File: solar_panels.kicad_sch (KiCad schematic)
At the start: 0 parts

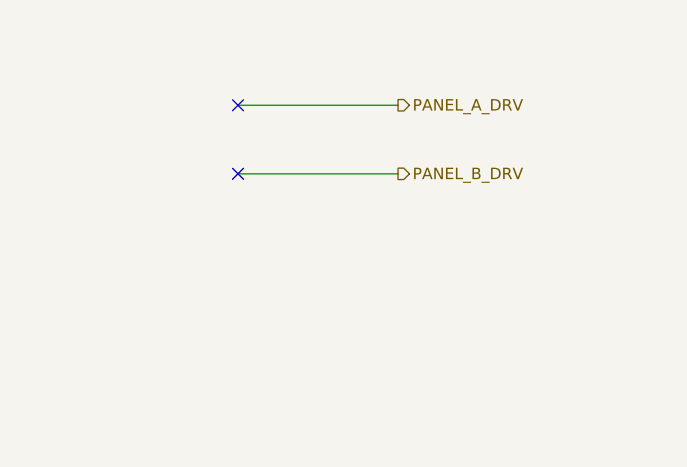
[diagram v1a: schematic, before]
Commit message: Adding in connections to schematic
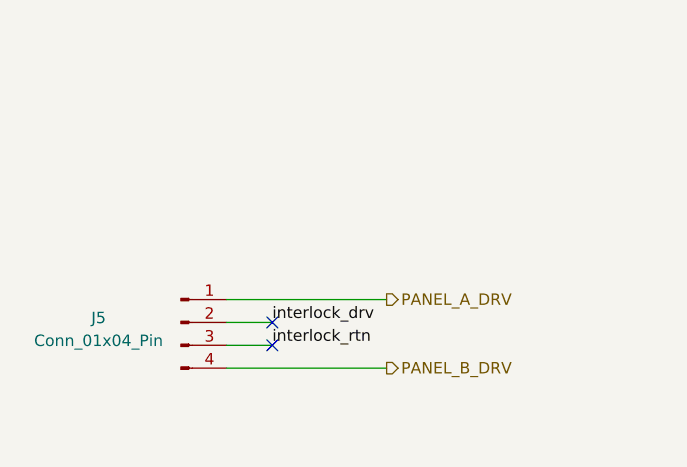
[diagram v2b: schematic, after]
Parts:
- added J5: Conn_01x04_Pin, symbol Connector:Conn_01x04_Pin
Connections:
- net PANEL_A_DRV: now also J5.1 (Pin_1)
- net PANEL_B_DRV: now also J5.4 (Pin_4)
- new net interlock_drv: J5.2 (Pin_2)
- new net interlock_rtn: J5.3 (Pin_3)
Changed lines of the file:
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@@
 	(paper "A4")
 	(no_connect
-		(at 134.62 73.66)
+		(at 138.43 97.79)
 	)
 	(no_connect
-		(at 134.62 81.28)
+		(at 138.43 100.33)
 	)
 	(wire
 		(pts
-			(xy 134.62 81.28) (xy 152.4 81.28)
+			(xy 133.35 102.87) (xy 151.13 102.87)
 		)
 		(stroke
@@
 	(wire
 		(pts
-			(xy 134.62 73.66) (xy 152.4 73.66)
+			(xy 133.35 95.25) (xy 151.13 95.25)
 		)
 		(stroke
@@
 		)
 	)
+	(wire
+		(pts
+			(xy 133.35 100.33) (xy 138.43 100.33)
+		)
+		(stroke
+			(width 0)
+			(type default)
+		)
+	)
+	(wire
+		(pts
+			(xy 133.35 97.79) (xy 138.43 97.79)
+		)
+		(stroke
+			(width 0)
+			(type default)
+		)
+	)
+	(label "interlock_drv"
+		(at 138.43 97.79 0)
+		(effects
+			(font
+				(size 1.27 1.27)
+			)
+			(justify left bottom)
+		)
+	)
+	(label "interlock_rtn"
+		(at 138.43 100.33 0)
+		(effects
+			(font
+				(size 1.27 1.27)
+			)
+			(justify left bottom)
+		)
+	)
 	(hierarchical_label "PANEL_A_DRV"
 		(shape output)
-		(at 152.4 73.66 0)
+		(at 151.13 95.25 0)
 		(effects
 			(font
@@
 	(hierarchical_label "PANEL_B_DRV"
 		(shape output)
-		(at 152.4 81.28 0)
+		(at 151.13 102.87 0)
 		(effects
 			(font
@@
 		)
 	)
+	(symbol
+		(lib_id "Connector:Conn_01x04_Pin")
+		(at 128.27 97.79 0)
+		(unit 1)
+		(exclude_from_sim no)
+		(in_bom yes)
+		(on_board yes)
+		(dnp no)
+		(property "Reference" "J5"
+			(at 119.126 97.282 0)
+			(effects
+				(font
+					(size 1.27 1.27)
+				)
+			)
+		)
+		(property "Value" "Conn_01x04_Pin"
+			(at 119.126 99.822 0)
+			(effects
+				(font
+					(size 1.27 1.27)
+				)
+			)
+		)
+		(property "Footprint" ""
+			(at 128.27 97.79 0)
+			(effects
+				(font
+					(size 1.27 1.27)
+				)
+				(hide yes)
+			)
+		)
+		(property "Datasheet" "~"
+			(at 128.27 97.79 0)
+			(effects
+				(font
+					(size 1.27 1.27)
+				)
+				(hide yes)
+			)
+		)
+		(property "Description" "Generic connector, single row, 01x04, script generated"
+			(at 128.27 97.79 0)
+			(effects
+				(font
+					(size 1.27 1.27)
+				)
+				(hide yes)
+			)
+		)
+		(pin "2"
+		)
+		(pin "1"
+		)
+		(pin "4"
+		)
+		(pin "3"
+		)
+		(instances
+			(project ""
+				(path "/99785679-20de-4827-b4cc-bc3c187068c9/9564929a-642e-4163-88c2-45054b63a5ed/84e96f9f-2d05-4b14-bccc-57bd87440548"
+					(reference "J5")
+					(unit 1)
+				)
+			)
+		)
+	)

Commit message: Working on layout now
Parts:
- renumbered J5 to J1
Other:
- company: (none) -> Solar Airplane
- title: (none) -> Solar Panel Connections
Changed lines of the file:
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@@
 	(generator_version "9.0")
 	(paper "A4")
+	(title_block
+		(title "Solar Panel Connections")
+		(rev "1")
+		(company "Solar Airplane")
+		(comment 1 "Engineer: Ezzat Suhaime")
+		(comment 2 "Reviewer 1: ")
+		(comment 3 "Reviewer 2:")
+	)
 	(no_connect
 		(at 138.43 97.79)
@@
 		(on_board yes)
 		(dnp no)
-		(property "Reference" "J5"
+		(property "Reference" "J1"
 			(at 119.126 97.282 0)
 			(effects
@@
 			(project ""
 				(path "/99785679-20de-4827-b4cc-bc3c187068c9/9564929a-642e-4163-88c2-45054b63a5ed/84e96f9f-2d05-4b14-bccc-57bd87440548"
-					(reference "J5")
+					(reference "J1")
 					(unit 1)
 				)

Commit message: Working on layout for dev board
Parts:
- added J6: Conn_01x04_Pin, symbol Connector:Conn_01x04_Pin
- J1: now not fitted; now left out of the parts list
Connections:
- net PANEL_A_DRV: now also J6.1 (Pin_1); no longer J1.1 (Pin_1)
- net PANEL_B_DRV: now also J1.1 (Pin_1); no longer J1.4 (Pin_4)
- net interlock_drv renamed interlock_B_drv
- net interlock_rtn renamed interlock_B_rtn
- new net GND: J1.4 (Pin_4), J6.4 (Pin_4)
- new net interlock_A_drv: J6.2 (Pin_2)
- new net interlock_A_rtn: J6.3 (Pin_3)
- no-connect marks 2 -> 4

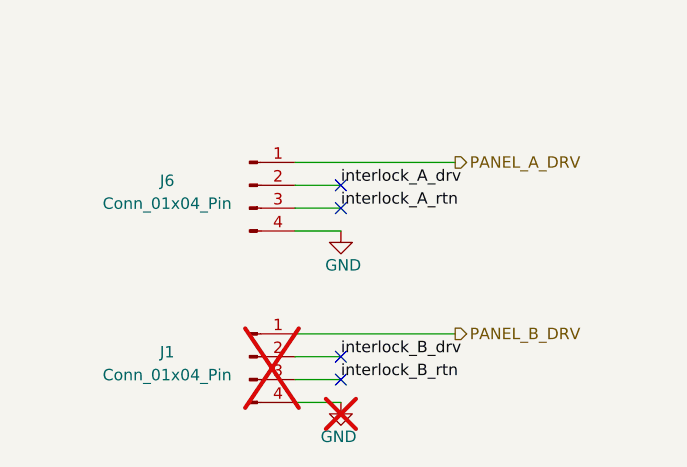
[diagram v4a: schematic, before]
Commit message: Working on layout. Adding in TPs to schematic
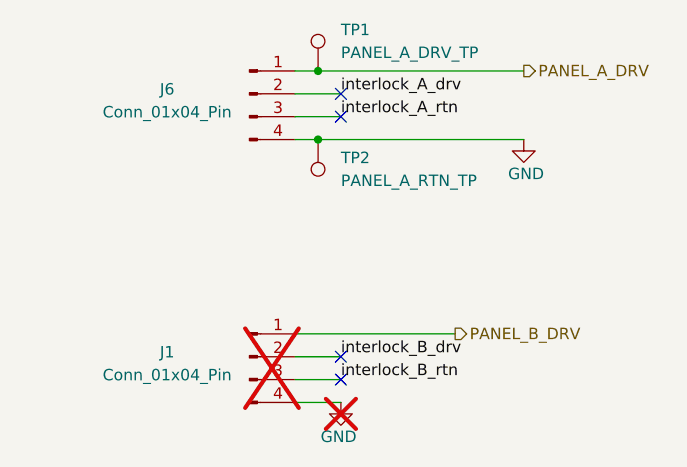
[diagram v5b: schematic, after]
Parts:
- added TP1: PANEL_A_DRV_TP, symbol Connector:TestPoint
- added TP2: PANEL_A_RTN_TP, symbol Connector:TestPoint
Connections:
- net GND: now also TP2.1
- net PANEL_A_DRV: now also TP1.1
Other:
- moved on the sheet: J6

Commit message: Finished with layout
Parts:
- J6: now not fitted; now left out of the parts list
- TP1, TP2: footprint (none) -> MountingHole:MountingHole_6mm_Pad_TopBottom
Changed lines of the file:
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@@
 			)
 		)
-		(property "Footprint" ""
+		(property "Footprint" "MountingHole:MountingHole_6mm_Pad_TopBottom"
 			(at 148.59 69.85 0)
 			(effects
@@
 			)
 		)
-		(property "Footprint" ""
+		(property "Footprint" "MountingHole:MountingHole_6mm_Pad_TopBottom"
 			(at 138.43 77.47 0)
 			(effects
@@
 		)
 		(property "Description" "test point"
+			(at 143.51 77.47 0)
+			(effects
+				(font
+					(size 1.27 1.27)
+				)
+				(hide yes)
+			)
+		)
+		(property "Mfr" ""
+			(at 143.51 77.47 0)
+			(effects
+				(font
+					(size 1.27 1.27)
+				)
+				(hide yes)
+			)
+		)
+		(property "Mfr P/N" ""
+			(at 143.51 77.47 0)
+			(effects
+				(font
+					(size 1.27 1.27)
+				)
+				(hide yes)
+			)
+		)
+		(property "Supplier_1" ""
+			(at 143.51 77.47 0)
+			(effects
+				(font
+					(size 1.27 1.27)
+				)
+				(hide yes)
+			)
+		)
+		(property "Supplier_1 P/N" ""
+			(at 143.51 77.47 0)
+			(effects
+				(font
+					(size 1.27 1.27)
+				)
+				(hide yes)
+			)
+		)
+		(property "Supplier_1 Unit Price" ""
+			(at 143.51 77.47 0)
+			(effects
+				(font
+					(size 1.27 1.27)
+				)
+				(hide yes)
+			)
+		)
+		(property "Supplier_1 Price @ Qty" ""
+			(at 143.51 77.47 0)
+			(effects
+				(font
+					(size 1.27 1.27)
+				)
+				(hide yes)
+			)
+		)
+		(property "Supplier_2" ""
+			(at 143.51 77.47 0)
+			(effects
+				(font
+					(size 1.27 1.27)
+				)
+				(hide yes)
+			)
+		)
+		(property "Supplier_2 P/N" ""
+			(at 143.51 77.47 0)
+			(effects
+				(font
+					(size 1.27 1.27)
+				)
+				(hide yes)
+			)
+		)
+		(property "Supplier_2 Unit Price" ""
+			(at 143.51 77.47 0)
+			(effects
+				(font
+					(size 1.27 1.27)
+				)
+				(hide yes)
+			)
+		)
+		(property "Supplier_2 Price @ Qty" ""
 			(at 143.51 77.47 0)
 			(effects
@@
 		(at 135.89 72.39 0)
 		(unit 1)
-		(exclude_from_sim no)
-		(in_bom yes)
-		(on_board yes)
-		(dnp no)
+		(exclude_from_sim yes)
+		(in_bom no)
+		(on_board no)
+		(dnp yes)
 		(property "Reference" "J6"
 			(at 126.746 71.882 0)

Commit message: Completing layout
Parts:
- renumbered J6 to J1, J1 to J2, TP1 to TP_IN_DRV1, TP2 to TP_IN_RTN1
